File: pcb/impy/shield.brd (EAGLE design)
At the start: 133 x 107 mm, 116 parts, among them J1 USB-2410-06, J2 SI-60062-F, J3 5V, U1 AD5933YRS, U10 LTC3406AB, U11 23LCV1024-I/SN, U12 MIC2009A-1YM6, U13 ADG725BSU, U14 ADG725BSU, U2 ADG704BRM, U3 AD8656ARZ, U4 M24C08WMN, U5 ADG706BRU, U6 DP83848I, U7 MIC2009A-1YM6, U8 AT25DF081A-SS, U9 SST25VF080B-80-4I-S2

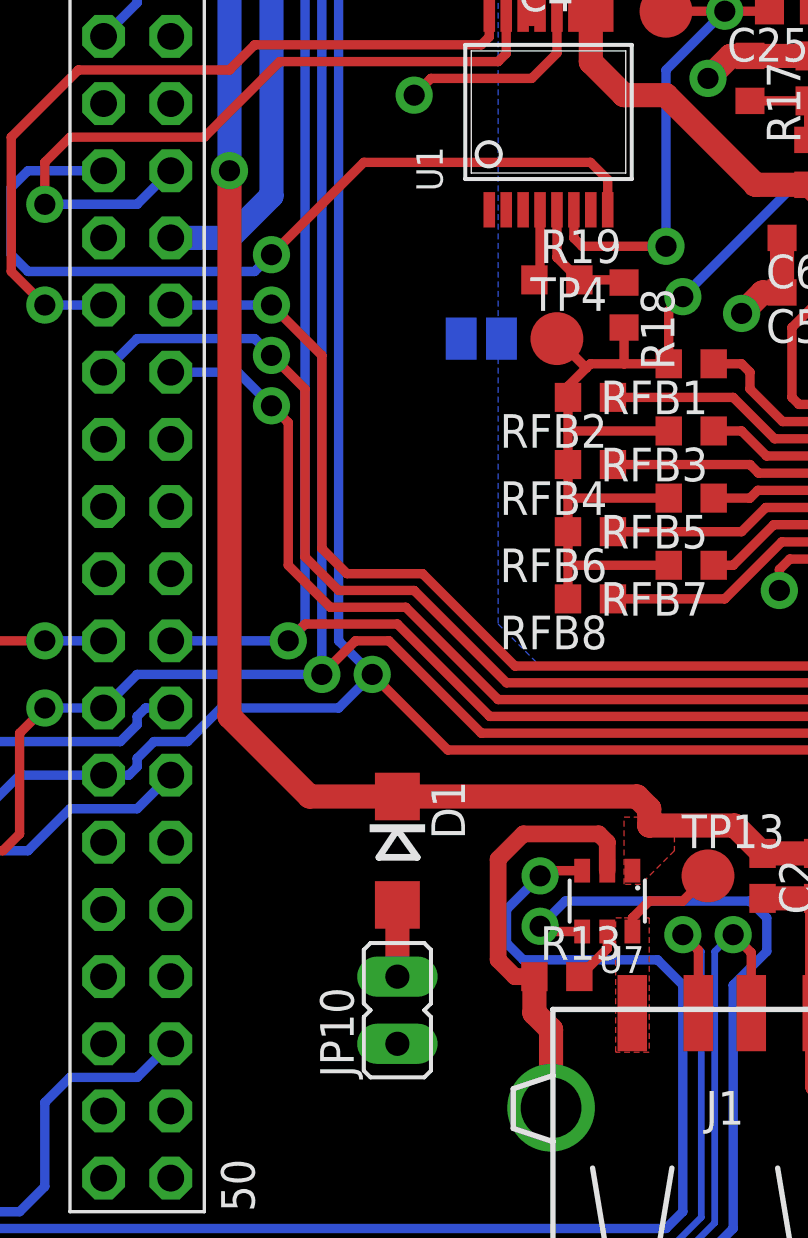
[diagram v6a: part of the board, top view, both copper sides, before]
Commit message: * pcb/impy: (shield.brd) Fix connection to jumper pins on top layer (cannot solder on top layer). Add missing connection that was previously removed.
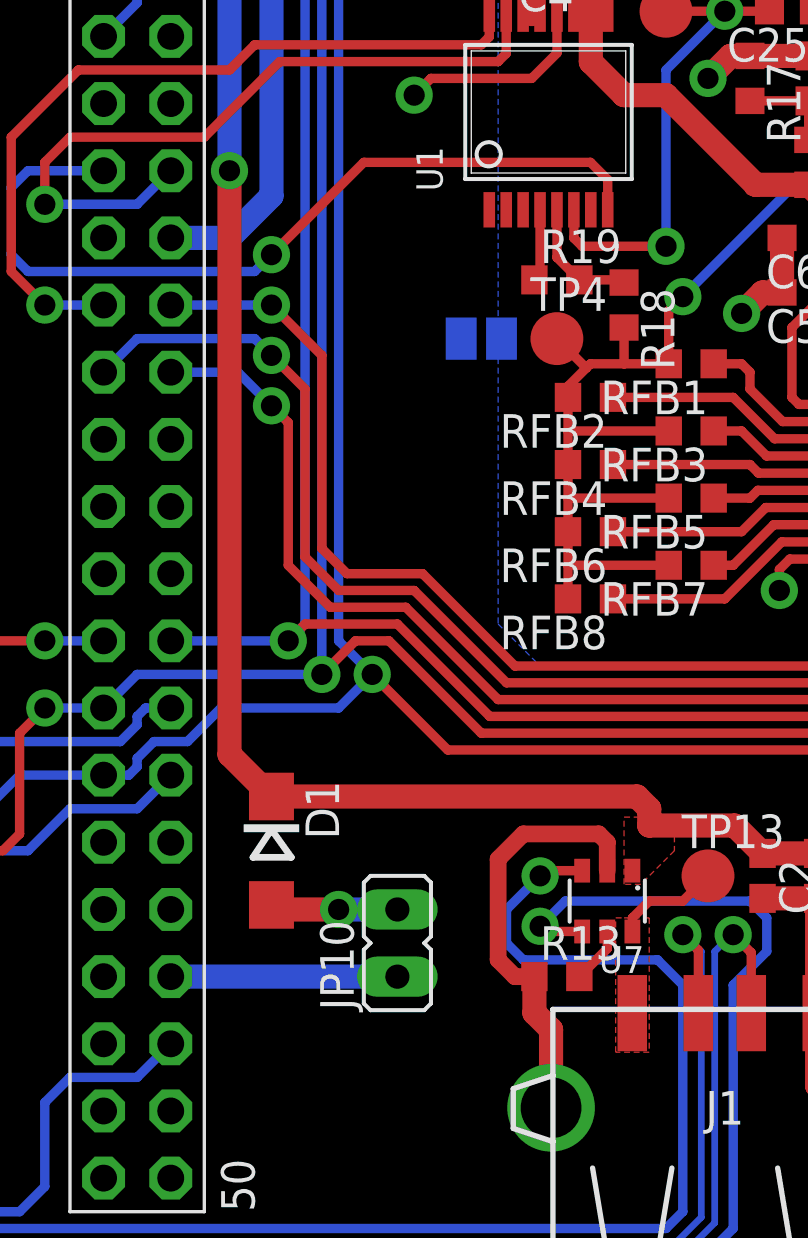
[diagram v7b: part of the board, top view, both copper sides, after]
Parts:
- moved D1 4.76 mm to (30.5, 14.9)
- moved JP10 2.54 mm to (35.2, 11.4)
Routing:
- net PA9: track 0.00 -> 8.57 mm
- net N$37: track 2.71 -> 4.83 mm, vias 0 -> 1
- net +5V: track 141.0 -> 141.9 mm
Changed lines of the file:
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@@
 <attribute name="RS" value="718-2455" x="36.83" y="-8.5725" size="1.778" layer="27" rot="R270" display="off"/>
 </element>
-<element name="JP10" library="jumper" package="JP1" value="VBUS" x="35.2425" y="8.89"/>
+<element name="JP10" library="jumper" package="JP1" value="VBUS" x="35.2425" y="11.43"/>
 <element name="J3" library="parts" package="JACK-SMD2.5" value="5V" x="49.8475" y="101.9175" rot="R270">
 <attribute name="RS" value="476-157" x="49.8475" y="101.9175" size="1.778" layer="27" rot="R270" display="off"/>
@@
 <attribute name="RS" value="727-4832" x="15.5575" y="41.275" size="1.778" layer="27" rot="R270" display="off"/>
 </element>
-<element name="D1" library="parts" package="DO214AC" value="STPS1L30A" x="35.2425" y="14.9225" rot="R270">
-<attribute name="RS" value="485-8061" x="35.2425" y="14.9225" size="1.778" layer="27" rot="R270" display="off"/>
+<element name="D1" library="parts" package="DO214AC" value="STPS1L30A" x="30.48" y="14.9225" rot="R270">
+<attribute name="RS" value="485-8061" x="30.48" y="14.9225" size="1.778" layer="27" rot="R270" display="off"/>
 </element>
 <element name="R12" library="rcl" package="R0603" value="510R" x="16.1925" y="43.815" rot="R180"/>
@@
 <wire x1="53.975" y1="13.335" x2="52.49" y2="14.82" width="0.3556" layer="1"/>
 <wire x1="52.49" y1="14.82" x2="51.1175" y2="14.82" width="0.3556" layer="1"/>
-<wire x1="28.8925" y1="20.0025" x2="31.9225" y2="16.9725" width="0.9144" layer="1"/>
-<wire x1="35.2425" y1="16.9725" x2="31.9225" y2="16.9725" width="0.9144" layer="1"/>
-<wire x1="35.2425" y1="16.9725" x2="44.305" y2="16.9725" width="0.9144" layer="1"/>
 <wire x1="44.305" y1="16.9725" x2="44.7675" y2="16.51" width="0.9144" layer="1"/>
-<wire x1="28.8925" y1="20.0025" x2="28.8925" y2="40.64" width="0.9144" layer="1"/>
+<wire x1="28.8925" y1="18.56" x2="28.8925" y2="40.64" width="0.9144" layer="1"/>
+<wire x1="28.8925" y1="18.56" x2="30.48" y2="16.9725" width="0.9144" layer="1"/>
+<wire x1="30.48" y1="16.9725" x2="44.305" y2="16.9725" width="0.9144" layer="1"/>
 </signal>
 <signal name="+3V3" class="1">
@@
 <contactref element="JP2" pad="44"/>
 <contactref element="JP10" pad="1"/>
-<wire x1="26.67" y1="10.16" x2="35.2425" y2="7.62" width="0" layer="19" extent="1-1"/>
+<wire x1="35.2425" y1="10.16" x2="26.67" y2="10.16" width="0.9144" layer="16"/>
 </signal>
 <signal name="PE2">
@@
 <contactref element="JP10" pad="2"/>
 <contactref element="D1" pad="A"/>
-<wire x1="35.2425" y1="10.16" x2="35.2425" y2="12.8725" width="0.9144" layer="1"/>
+<wire x1="35.2425" y1="12.7" x2="33.02" y2="12.7" width="0.9144" layer="16"/>
+<via x="33.02" y="12.7" extent="1-16" drill="0.8" shape="octagon"/>
+<wire x1="33.02" y1="12.7" x2="30.6525" y2="12.7" width="0.9144" layer="1"/>
+<wire x1="30.6525" y1="12.7" x2="30.48" y2="12.8725" width="0.9144" layer="1"/>
 </signal>
 <signal name="N$38">

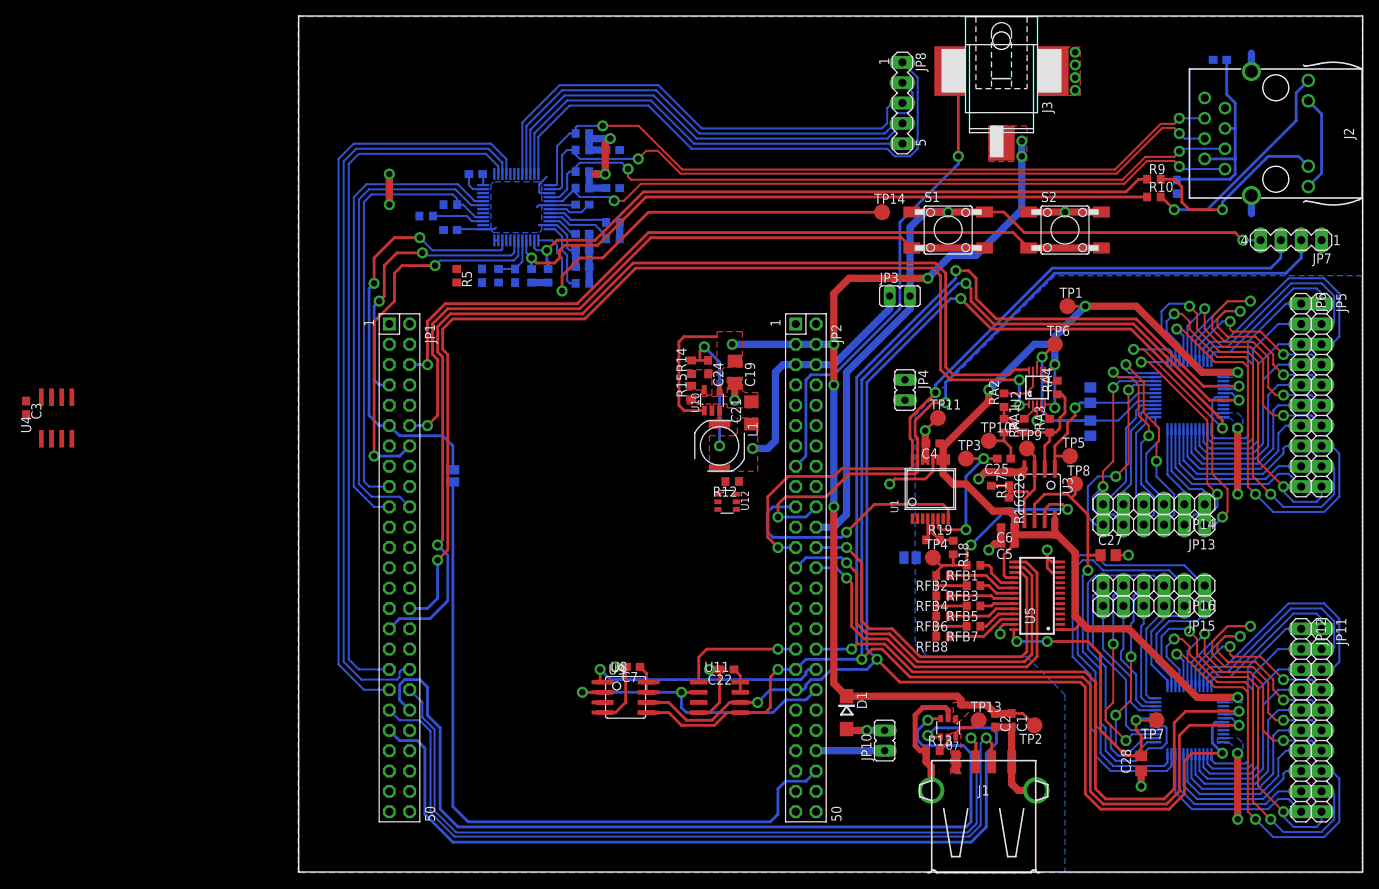
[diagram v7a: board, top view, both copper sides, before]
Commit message: * pcb/impy: (shield.sch) Change attenuation mux signals (PE12, PE13 to PE5, PE6).   (shield.brd) Layout new attenuation mux signals. Optimize layout of +5V and I2C.
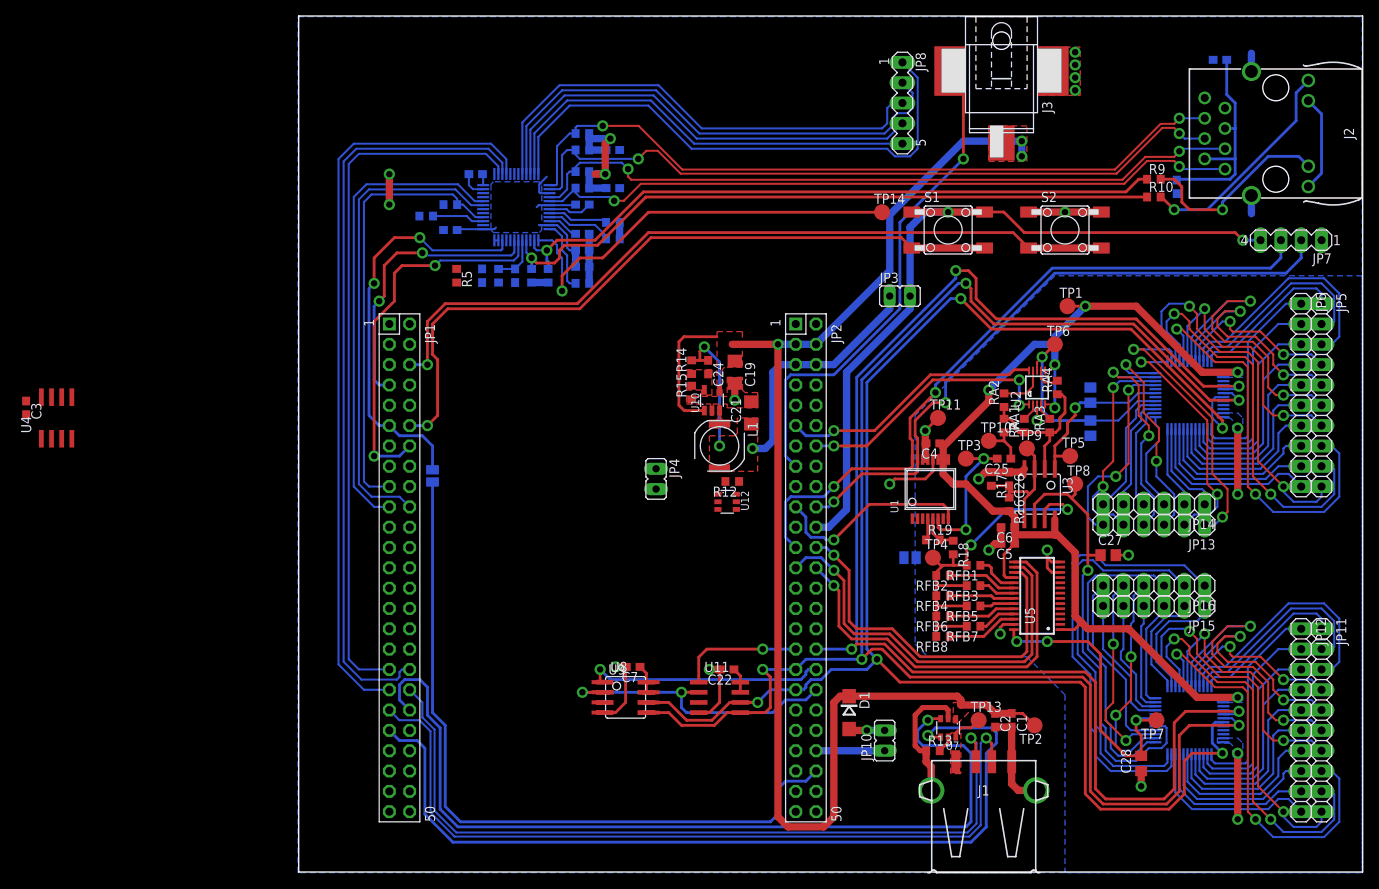
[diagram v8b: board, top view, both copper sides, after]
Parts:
- moved JP4 33.0 mm to (6.67, 44.1)
- moved SJ2 2.54 mm to (-21.3, 44.5)
- moved D1 0.32 mm to (30.8, 14.9)
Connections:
- removed net PE12: JP1.30, U2.1
- removed net PE13: JP1.31, U2.10
- new net PE5: JP2.14, U2.1
- new net PE6: JP2.11, U2.10
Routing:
- net PE13: track 134.3 -> 0.00 mm, vias 1 -> 0
- net PE12: track 130.8 -> 0.00 mm, vias 3 -> 0
- net +5V: track 141.9 -> 177.8 mm, vias 7 -> 3
- net PE5: track 0.00 -> 33.3 mm, vias 0 -> 3
- net PE6: track 0.00 -> 33.2 mm, vias 0 -> 1
- net PB9: track 92.9 -> 81.4 mm
- net PB8: track 32.2 -> 25.1 mm
- net PB6: track 92.3 -> 87.5 mm
- net PE2: track 59.9 -> 63.0 mm
- net ETH_CLK: track 53.9 -> 51.3 mm
- net PC12: track 203.6 -> 205.5 mm
- net PC9: track 91.3 -> 92.9 mm
- net PB7: track 47.7 -> 47.1 mm
- net PB5: track 50.4 -> 49.8 mm
- net PB4: track 52.1 -> 51.5 mm
